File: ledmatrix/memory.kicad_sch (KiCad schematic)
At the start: 8 parts, among them U16 74LS32, U23 74HC138, U24 LC36128ML, U25 27C1000DC-12, U4 74HC14

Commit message: switch to desktop
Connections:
- net PIN16(~{CONCS}) renamed PIN16(~{IORQ})
- net PIN33(CONCS) renamed PIN33(~{M1})
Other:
- note added: "No idea what the point of this is. Both these pins _only_ connect to these gates. So why not do this in software. edit: probably because it's for the IO request. /iorq goes low, and /M1 goes high during an io request"
- note removed: "No idea what the point of this is. Both these pins _only_ connect to these gates. So why not do this in software."
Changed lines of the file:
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@@
     (effects (font (size 1.27 1.27)) (justify left bottom))
   )
-  (text "No idea what the point of this is.\nBoth these pins _only_ connect to these gates.\nSo why not do this in software.\n"
+  (text "No idea what the point of this is.\nBoth these pins _only_ connect to these gates.\nSo why not do this in software.\n\nedit: probably because it's for the IO request.\n/iorq goes low, and /M1 goes high during an io request\n\n"
     (at 86.36 90.17 0)
     (effects (font (size 1.27 1.27)) (justify left bottom))
@@
     (effects (font (size 1.27 1.27)) (justify left))
   )
-  (hierarchical_label "PIN33(CONCS)" (shape input) (at 92.71 102.87 180)
+  (hierarchical_label "PIN33(~{M1})" (shape input) (at 92.71 102.87 180)
     (effects (font (size 1.27 1.27)) (justify right))
   )
@@
     (effects (font (size 1.27 1.27)) (justify left))
   )
-  (hierarchical_label "PIN16(~{CONCS})" (shape input) (at 92.71 92.71 180)
+  (hierarchical_label "PIN16(~{IORQ})" (shape input) (at 92.71 92.71 180)
     (effects (font (size 1.27 1.27)) (justify right))
   )

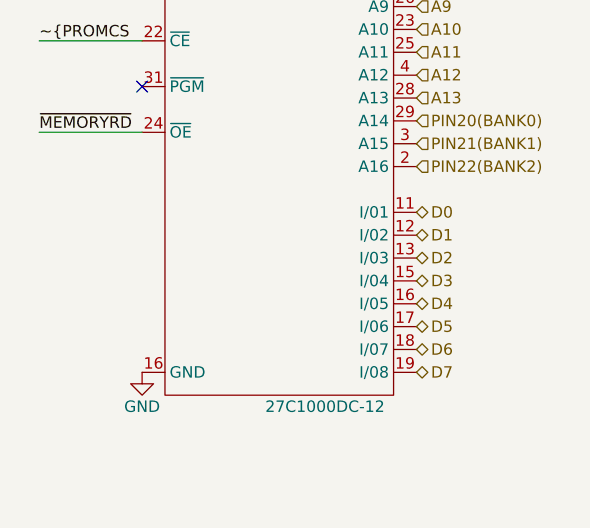
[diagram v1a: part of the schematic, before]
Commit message: Work on led matrix display.
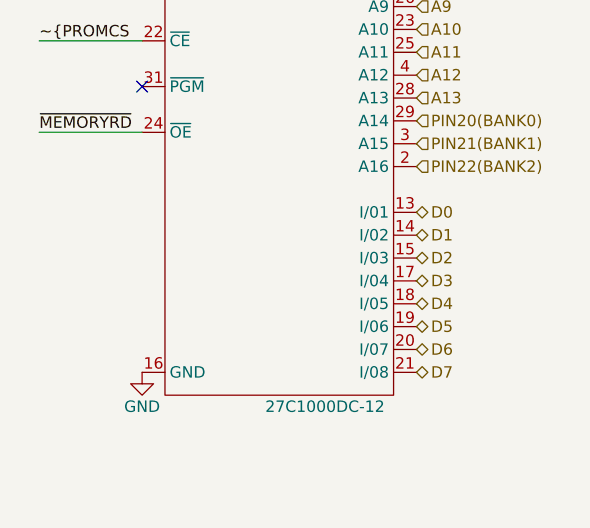
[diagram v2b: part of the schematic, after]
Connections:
- net D0: now also U25.13 (I/01); no longer U25.11 (I/01)
- net D1: now also U25.14 (I/02); no longer U25.12 (I/02)
- net D2: now also U25.15 (I/03); no longer U25.13 (I/03)
- net D3: now also U25.17 (I/04); no longer U25.15 (I/04)
- net D4: now also U25.18 (I/05); no longer U25.16 (I/05)
- net D5: now also U25.19 (I/06); no longer U25.17 (I/06)
- net D6: now also U25.20 (I/07); no longer U25.18 (I/07)
- net D7: now also U25.21 (I/08); no longer U25.19 (I/08)
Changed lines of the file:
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@@
     (pin "10")
     (pin "11")
-    (pin "11")
-    (pin "12")
     (pin "12")
     (pin "13")
+    (pin "14")
     (pin "15")
-    (pin "16")
     (pin "16")
     (pin "17")
@@
     (pin "19")
     (pin "2")
+    (pin "20")
+    (pin "21")
     (pin "22")
     (pin "23")
